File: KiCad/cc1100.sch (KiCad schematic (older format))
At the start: 21 parts

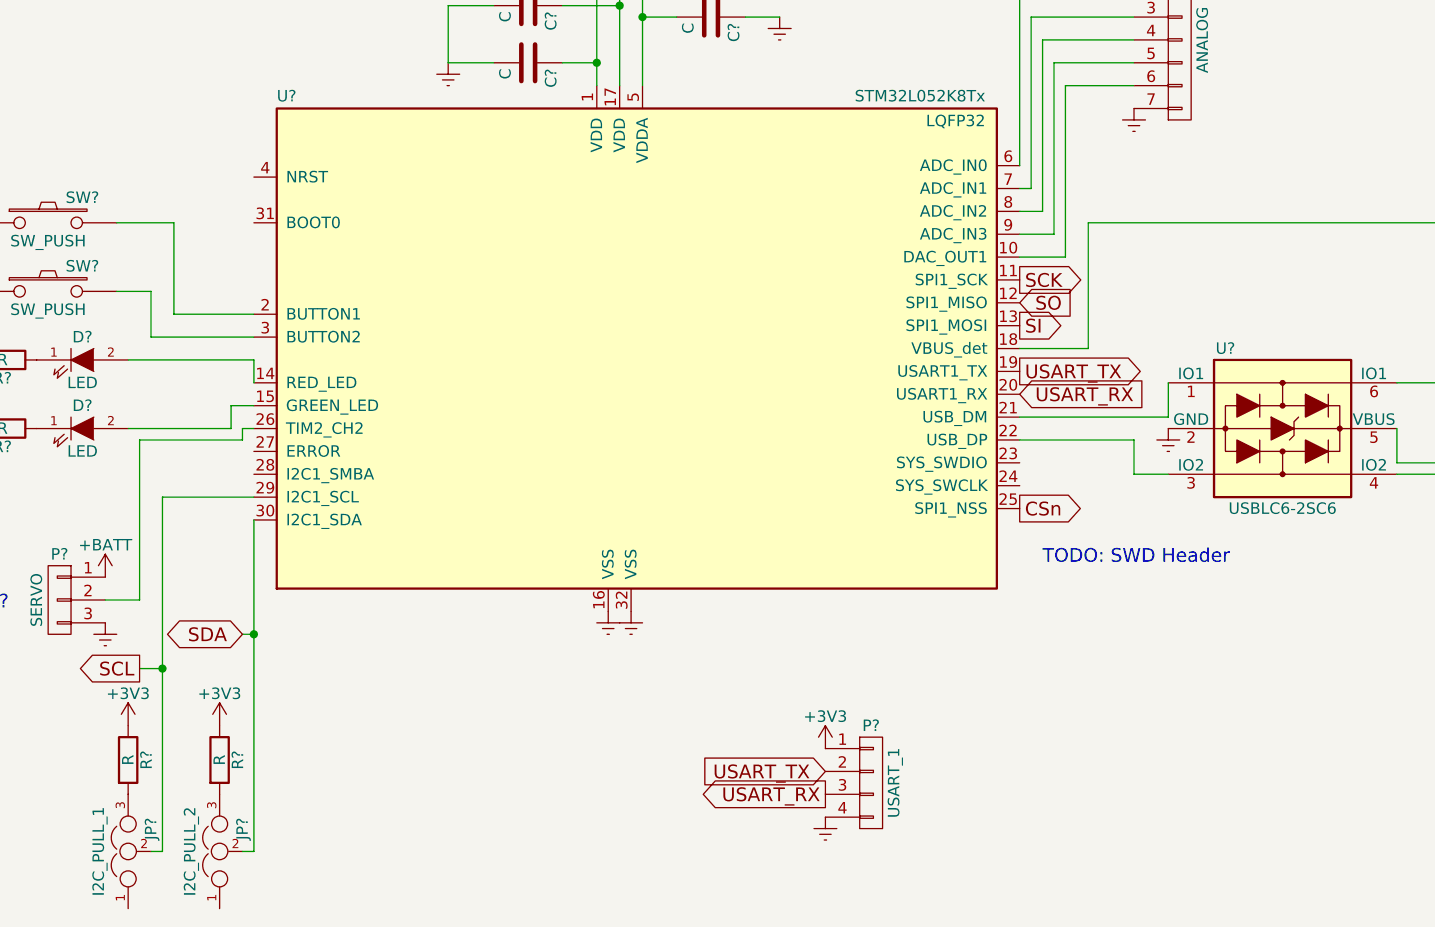
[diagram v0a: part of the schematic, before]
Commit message: Added SWD port
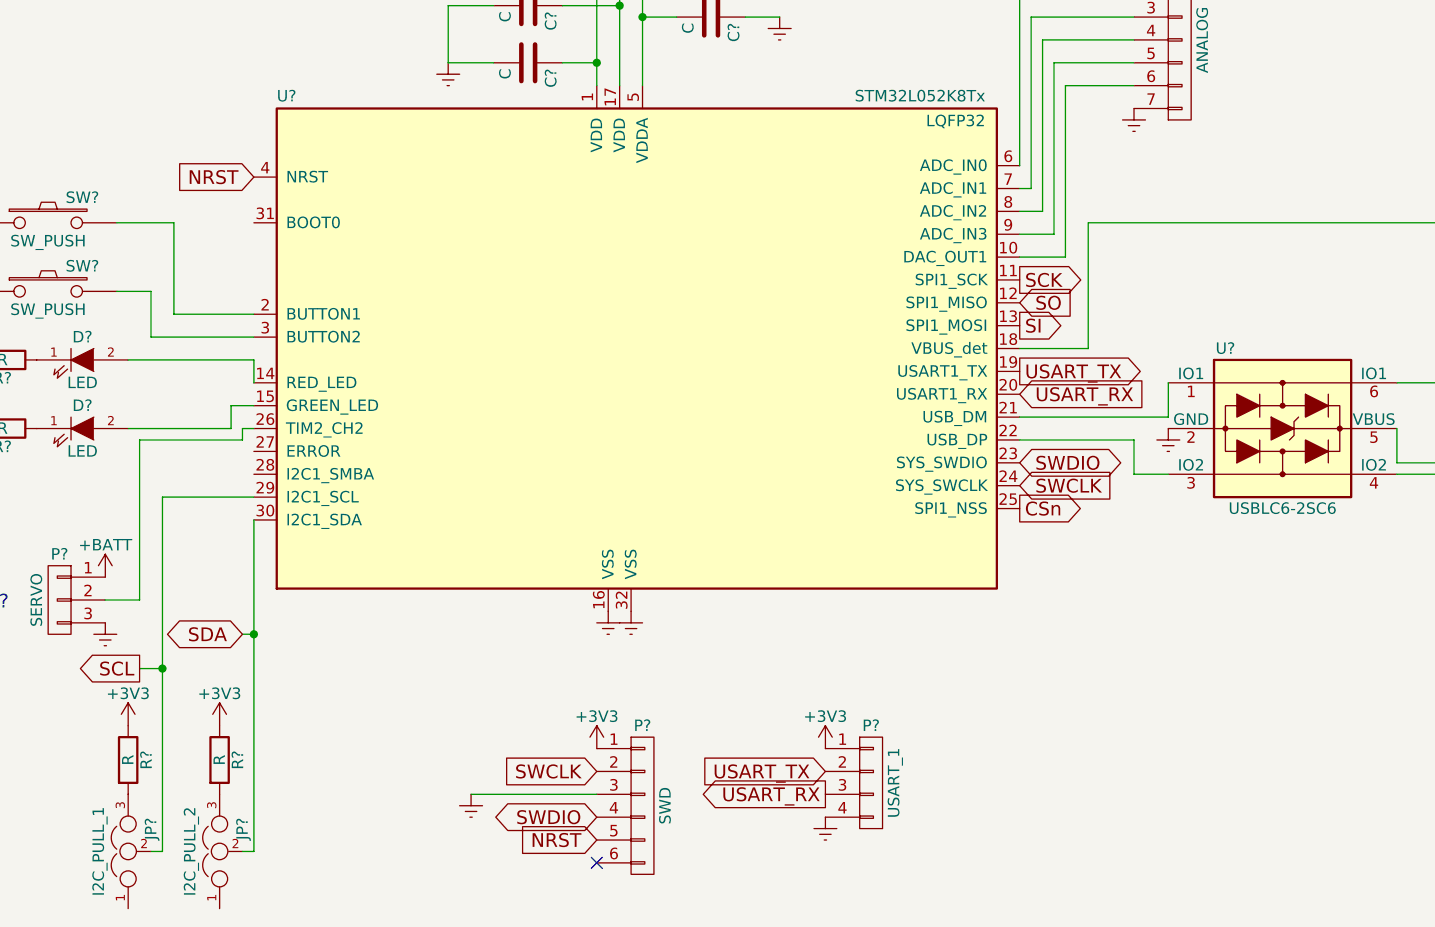
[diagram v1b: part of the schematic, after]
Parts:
- added P?: SWD, symbol CONN_01X06
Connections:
- net +3V3: now also P?.1 (P1)
- net Earth: now also P?.3 (P3)
- net SWDIO: now reaches U?.23 (SYS_SWDIO)
- net SWDIO: now also P?.4 (P4)
- net SWCLK: now reaches U?.24 (SYS_SWCLK)
- net SWCLK: now also P?.2 (P2)
- net NRST: now reaches U?.4 (NRST)
- net NRST: now also P?.5 (P5)
- no-connect marks 0 -> 1
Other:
- note removed: "TODO: SWD Header"
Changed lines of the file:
@@
 Text Notes 2050 6300 0    60   ~ 0
 TODO: MOSFET?
-Text Notes 7250 6100 0    60   ~ 0
-TODO: SWD Header
 Text Notes 3800 3450 0    60   ~ 0
 TODO: More decoupling?
+$Comp
+L CONN_01X06 P?
+U 1 1 5810EFB0
+P 5500 7150
+F 0 "P?" H 5500 7500 50  0000 C CNN
+F 1 "SWD" V 5600 7150 50  0000 C CNN
+F 2 "" H 5500 7150 50  0000 C CNN
+F 3 "" H 5500 7150 50  0000 C CNN
+	1    5500 7150
+	1    0    0    -1
+$EndComp
+$Comp
+L +3V3 #PWR?
+U 1 1 5810F2C2
+P 5300 6900
+F 0 "#PWR?" H 5300 6750 50  0001 C CNN
+F 1 "+3V3" H 5300 7040 50  0000 C CNN
+F 2 "" H 5300 6900 50  0000 C CNN
+F 3 "" H 5300 6900 50  0000 C CNN
+	1    5300 6900
+	1    0    0    -1
+$EndComp
+Text GLabel 7150 5750 2    60   Input ~ 0
+SWCLK
+Text GLabel 7150 5650 2    60   BiDi ~ 0
+SWDIO
+Text GLabel 5300 7200 0    60   BiDi ~ 0
+SWDIO
+Text GLabel 5300 7000 0    60   Input ~ 0
+SWCLK
+$Comp
+L Earth #PWR?
+U 1 1 5810F450
+P 4750 7100
+F 0 "#PWR?" H 4750 6850 50  0001 C CNN
+F 1 "Earth" H 4750 6950 50  0001 C CNN
+F 2 "" H 4750 7100 50  0000 C CNN
+F 3 "" H 4750 7100 50  0000 C CNN
+	1    4750 7100
+	1    0    0    -1
+$EndComp
+Wire Wire Line
+	4750 7100 5300 7100
+Text GLabel 3800 4400 0    60   Input ~ 0
+NRST
+Text GLabel 5300 7300 0    60   Input ~ 0
+NRST
+NoConn ~ 5300 7400
 $EndSCHEMATC

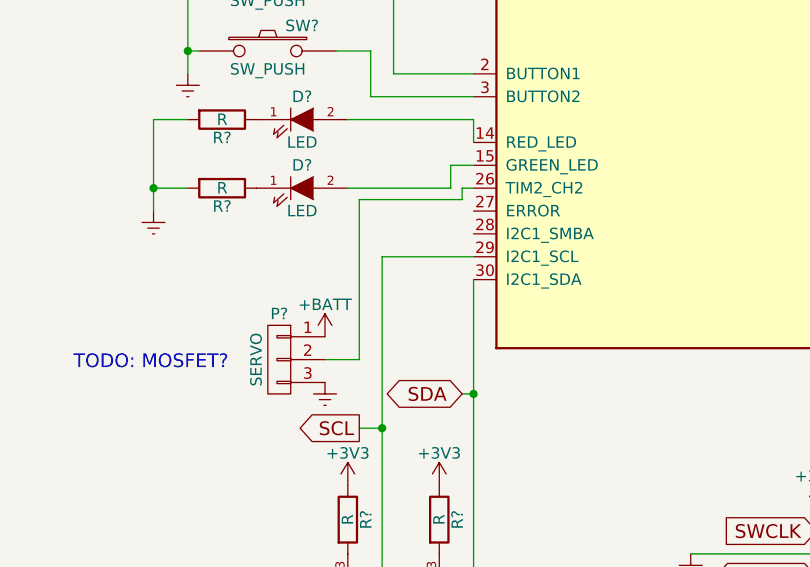
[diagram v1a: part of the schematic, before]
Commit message: Added SMBus Alert pin for TMP112
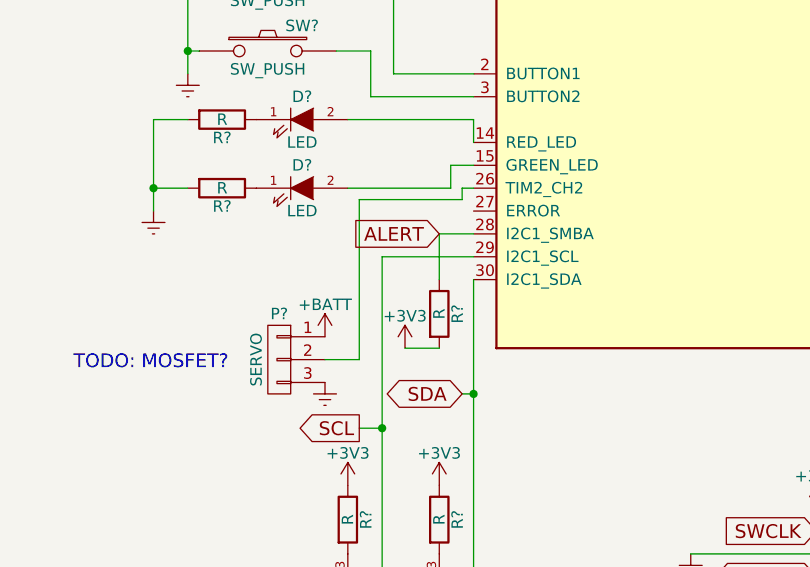
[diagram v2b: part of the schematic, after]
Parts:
- added R?: R, symbol R
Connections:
- net +3V3: now also R?.2
- net ALERT: now reaches U?.28 (I2C1_SMBA)
- net ALERT: now also R?.1
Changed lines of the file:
@@
 NRST
 NoConn ~ 5300 7400
+$Comp
+L R R?
+U 1 1 581106B3
+P 3650 6050
+F 0 "R?" V 3730 6050 50  0000 C CNN
+F 1 "R" V 3650 6050 50  0000 C CNN
+F 2 "" V 3580 6050 50  0000 C CNN
+F 3 "" H 3650 6050 50  0000 C CNN
+	1    3650 6050
+	1    0    0    -1
+$EndComp
+$Comp
+L +3V3 #PWR?
+U 1 1 5811071B
+P 3500 6200
+F 0 "#PWR?" H 3500 6050 50  0001 C CNN
+F 1 "+3V3" H 3500 6340 50  0000 C CNN
+F 2 "" H 3500 6200 50  0000 C CNN
+F 3 "" H 3500 6200 50  0000 C CNN
+	1    3500 6200
+	1    0    0    -1
+$EndComp
+Text GLabel 3650 5700 0    60   Input ~ 0
+ALERT
+Wire Wire Line
+	3500 6200 3650 6200
+Wire Wire Line
+	3650 5900 3650 5700
+Wire Wire Line
+	3650 5700 3800 5700
 $EndSCHEMATC

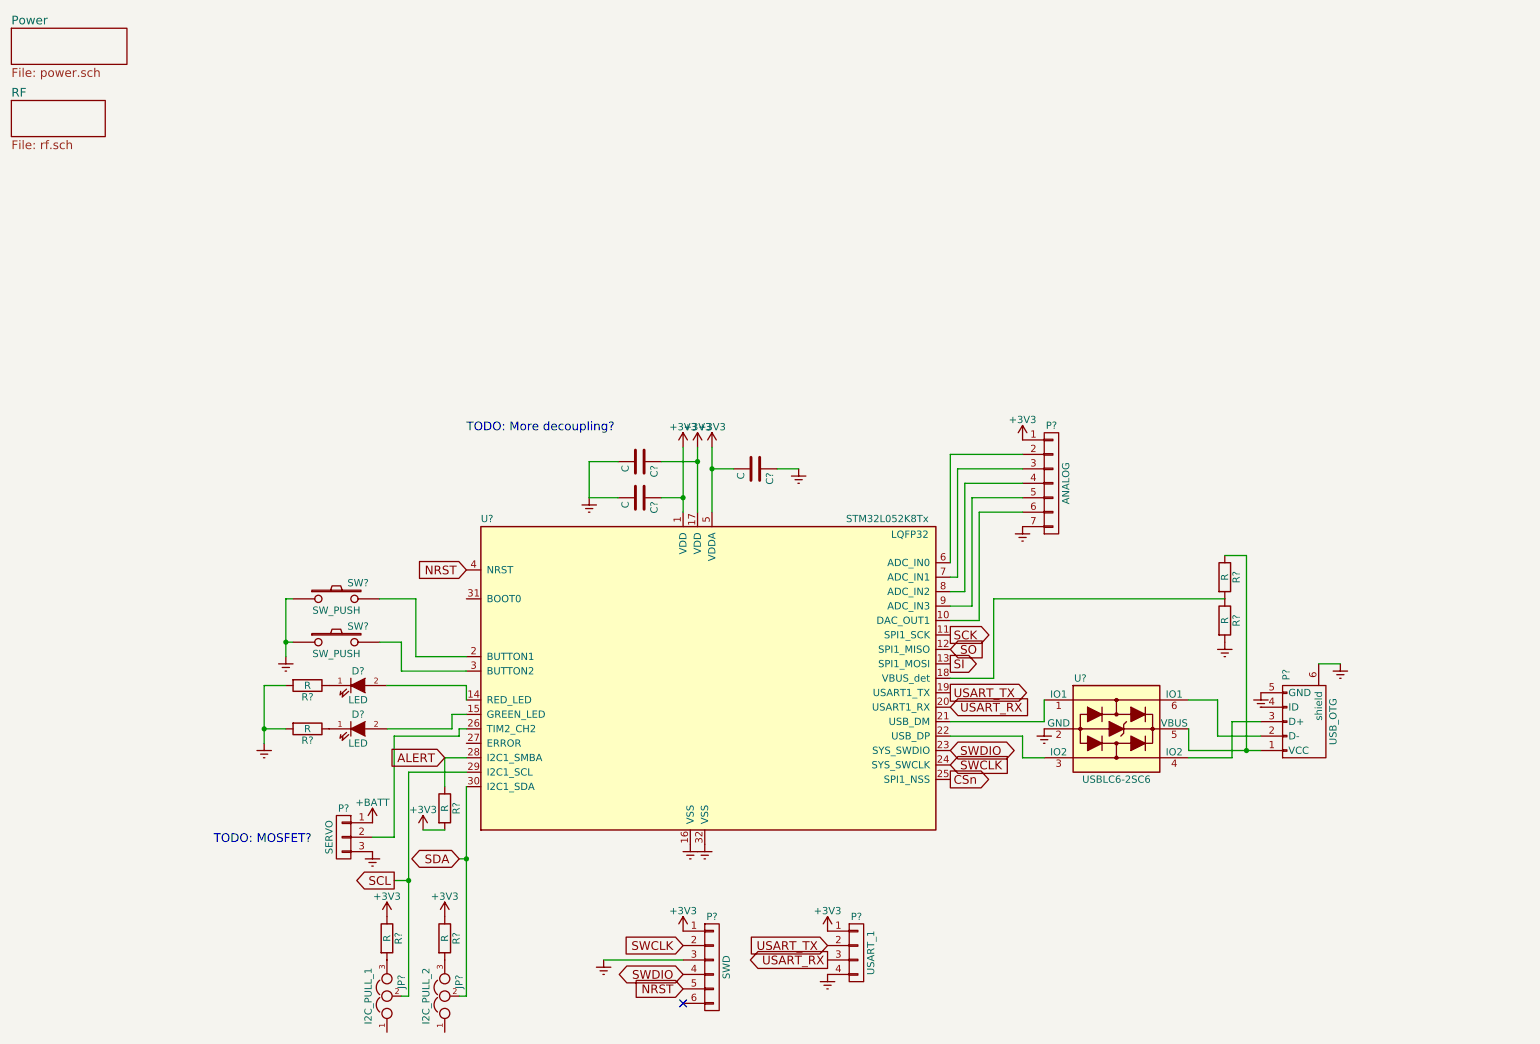
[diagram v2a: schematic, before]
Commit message: Added edge connector and UART leveler
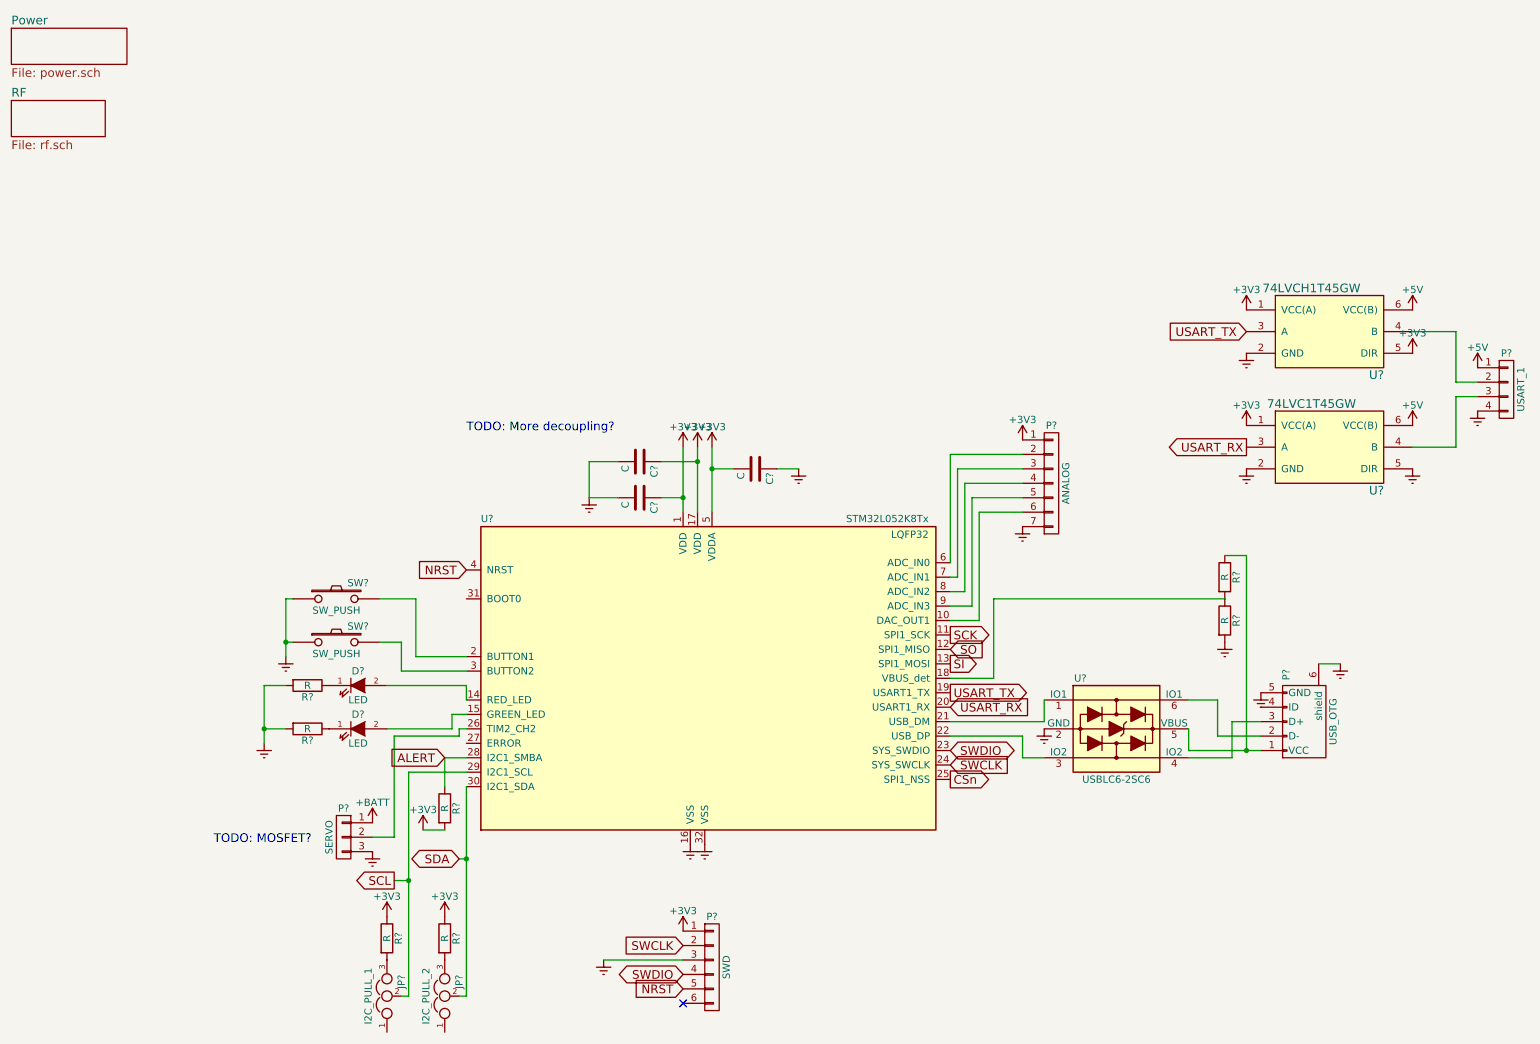
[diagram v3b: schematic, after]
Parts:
- added U?: 74LVCH1T45GW, symbol 74LVCH1T45GW
- added U?: 74LVC1T45GW, symbol 74LVC1T45GW
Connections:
- net +3V3: now also U?.1 (VCC(A)), U?.1 (VCC(A)), U?.5 (DIR); no longer P?.1 (P1)
- net Earth: now also U?.2 (GND), U?.2 (GND), U?.5 (DIR)
- net USART_RX: now also U?.3 (A); no longer P?.3 (P3)
- net USART_TX: now also U?.3 (A); no longer P?.2 (P2)
- new net: P?.2 (P2), U?.4 (B)
- new net: P?.3 (P3), U?.4 (B)
- new net +5V: P?.1 (P1), U?.6 (VCC(B)), U?.6 (VCC(B))
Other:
- moved on the sheet: P?
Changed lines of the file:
@@
 LIBS:Xicor
 LIBS:Zilog
+LIBS:sma_edge
 LIBS:cc1100-cache
 EELAYER 25 0
@@
 L CONN_01X04 P?
 U 1 1 5810F5E5
-P 6500 7050
-F 0 "P?" H 6500 7300 50  0000 C CNN
-F 1 "USART_1" V 6600 7050 50  0000 C CNN
-F 2 "" H 6500 7050 50  0000 C CNN
-F 3 "" H 6500 7050 50  0000 C CNN
-	1    6500 7050
+P 11000 3150
+F 0 "P?" H 11000 3400 50  0000 C CNN
+F 1 "USART_1" V 11100 3150 50  0000 C CNN
+F 2 "" H 11000 3150 50  0000 C CNN
+F 3 "" H 11000 3150 50  0000 C CNN
+	1    11000 3150
 	1    0    0    -1
 $EndComp
@@
 L Earth #PWR018
 U 1 1 5810F65D
-P 6300 7200
-F 0 "#PWR018" H 6300 6950 50  0001 C CNN
-F 1 "Earth" H 6300 7050 50  0001 C CNN
-F 2 "" H 6300 7200 50  0000 C CNN
-F 3 "" H 6300 7200 50  0000 C CNN
-	1    6300 7200
-	1    0    0    -1
-$EndComp
-$Comp
-L +3V3 #PWR019
-U 1 1 5810F6A4
-P 6300 6900
-F 0 "#PWR019" H 6300 6750 50  0001 C CNN
-F 1 "+3V3" H 6300 7040 50  0000 C CNN
-F 2 "" H 6300 6900 50  0000 C CNN
-F 3 "" H 6300 6900 50  0000 C CNN
-	1    6300 6900
+P 10800 3300
+F 0 "#PWR018" H 10800 3050 50  0001 C CNN
+F 1 "Earth" H 10800 3150 50  0001 C CNN
+F 2 "" H 10800 3300 50  0000 C CNN
+F 3 "" H 10800 3300 50  0000 C CNN
+	1    10800 3300
 	1    0    0    -1
 $EndComp
@@
 USART_TX
 Text GLabel 7150 5350 2    60   Input ~ 0
-USART_RX
-Text GLabel 6300 7000 0    60   Input ~ 0
-USART_TX
-Text GLabel 6300 7100 0    60   Output ~ 0
 USART_RX
 $Comp
@@
 Wire Wire Line
 	3650 5700 3800 5700
+$Comp
+L 74LVCH1T45GW U?
+U 1 1 581E3B9C
+P 9750 2750
+F 0 "U?" H 10100 2450 60  0000 C CNN
+F 1 "74LVCH1T45GW" H 9650 3050 60  0000 C CNN
+F 2 "" H 9900 2600 60  0001 C CNN
+F 3 "" H 9900 2600 60  0001 C CNN
+	1    9750 2750
+	1    0    0    -1
+$EndComp
+$Comp
+L 74LVC1T45GW U?
+U 1 1 581E3C1B
+P 9750 3550
+F 0 "U?" H 10100 3250 60  0000 C CNN
+F 1 "74LVC1T45GW" H 9650 3850 60  0000 C CNN
+F 2 "" H 9900 3400 60  0001 C CNN
+F 3 "" H 9900 3400 60  0001 C CNN
+	1    9750 3550
+	1    0    0    -1
+$EndComp
+Text GLabel 9200 2750 0    60   Input ~ 0
+USART_TX
+Text GLabel 9200 3550 0    60   Output ~ 0
+USART_RX
+$Comp
+L Earth #PWR?
+U 1 1 581E3E6B
+P 9200 2900
+F 0 "#PWR?" H 9200 2650 50  0001 C CNN
+F 1 "Earth" H 9200 2750 50  0001 C CNN
+F 2 "" H 9200 2900 50  0000 C CNN
+F 3 "" H 9200 2900 50  0000 C CNN
+	1    9200 2900
+	1    0    0    -1
+$EndComp
+$Comp
+L Earth #PWR?
+U 1 1 581E3ECA
+P 9200 3700
+F 0 "#PWR?" H 9200 3450 50  0001 C CNN
+F 1 "Earth" H 9200 3550 50  0001 C CNN
+F 2 "" H 9200 3700 50  0000 C CNN
+F 3 "" H 9200 3700 50  0000 C CNN
+	1    9200 3700
+	1    0    0    -1
+$EndComp
+$Comp
+L +5V #PWR?
+U 1 1 581E3F29
+P 10800 3000
+F 0 "#PWR?" H 10800 2850 50  0001 C CNN
+F 1 "+5V" H 10800 3140 50  0000 C CNN
+F 2 "" H 10800 3000 50  0000 C CNN
+F 3 "" H 10800 3000 50  0000 C CNN
+	1    10800 3000
+	1    0    0    -1
+$EndComp
+$Comp
+L +5V #PWR?
+U 1 1 581E4012
+P 10350 3400
+F 0 "#PWR?" H 10350 3250 50  0001 C CNN
+F 1 "+5V" H 10350 3540 50  0000 C CNN
+F 2 "" H 10350 3400 50  0000 C CNN
+F 3 "" H 10350 3400 50  0000 C CNN
+	1    10350 3400
+	1    0    0    -1
+$EndComp
+$Comp
+L +5V #PWR?
+U 1 1 581E4071
+P 10350 2600
+F 0 "#PWR?" H 10350 2450 50  0001 C CNN
+F 1 "+5V" H 10350 2740 50  0000 C CNN
+F 2 "" H 10350 2600 50  0000 C CNN
+F 3 "" H 10350 2600 50  0000 C CNN
+	1    10350 2600
+	1    0    0    -1
+$EndComp
+$Comp
+L +3V3 #PWR?
+U 1 1 581E40D0
+P 9200 2600
+F 0 "#PWR?" H 9200 2450 50  0001 C CNN
+F 1 "+3V3" H 9200 2740 50  0000 C CNN
+F 2 "" H 9200 2600 50  0000 C CNN
+F 3 "" H 9200 2600 50  0000 C CNN
+	1    9200 2600
+	1    0    0    -1
+$EndComp
+$Comp
+L +3V3 #PWR?
+U 1 1 581E4148
+P 9200 3400
+F 0 "#PWR?" H 9200 3250 50  0001 C CNN
+F 1 "+3V3" H 9200 3540 50  0000 C CNN
+F 2 "" H 9200 3400 50  0000 C CNN
+F 3 "" H 9200 3400 50  0000 C CNN
+	1    9200 3400
+	1    0    0    -1
+$EndComp
+Wire Wire Line
+	10350 2750 10650 2750
+Wire Wire Line
+	10650 2750 10650 3100
+Wire Wire Line
+	10650 3100 10800 3100
+Wire Wire Line
+	10350 3550 10650 3550
+Wire Wire Line
+	10650 3550 10650 3200
+Wire Wire Line
+	10650 3200 10800 3200
+$Comp
+L Earth #PWR?
+U 1 1 581E4537
+P 10350 3700
+F 0 "#PWR?" H 10350 3450 50  0001 C CNN
+F 1 "Earth" H 10350 3550 50  0001 C CNN
+F 2 "" H 10350 3700 50  0000 C CNN
+F 3 "" H 10350 3700 50  0000 C CNN
+	1    10350 3700
+	1    0    0    -1
+$EndComp
+$Comp
+L +3V3 #PWR?
+U 1 1 581E4596
+P 10350 2900
+F 0 "#PWR?" H 10350 2750 50  0001 C CNN
+F 1 "+3V3" H 10350 3040 50  0000 C CNN
+F 2 "" H 10350 2900 50  0000 C CNN
+F 3 "" H 10350 2900 50  0000 C CNN
+	1    10350 2900
+	1    0    0    -1
+$EndComp
 $EndSCHEMATC
